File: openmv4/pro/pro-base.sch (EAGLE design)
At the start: 154 parts, among them J2 SAMTEC_FTSH-105-01-F-DVSAMTEC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, J6 2337019-1, M1 9774030243R, M2 9774030243R, Q1 BSS138, Q2 AO3401, U1 W25Q256JVEIQ_TR, U10 STM32H743IIK6, U11 TEXAS_INSTRUMENTS_BQ24072TRGT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, U14 IS42S32800, U2 EMIF06-MSD02N16, U3 ME6211C18M5G, U4 PAM2305AABADJ, U5 LSM6DS3TR-C, U6 MICROCHIP_USB3320C-EZK-TRMICR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, U7 LBEE5KL1DX-TEMP, U8 STMICROELECTRONICS_VL53L1CXV0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, U9 NXP_SEMICONDUCTORS_SE050C2HQ1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, X2 USD-1040310811, X3 DF12-36-DS, X4 S2B-PH-K-S(LF)(SN), Y0 SITIME_SIT1533AI-H4-DCC-32.76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, Y1 DSC1001BI1-024.0000

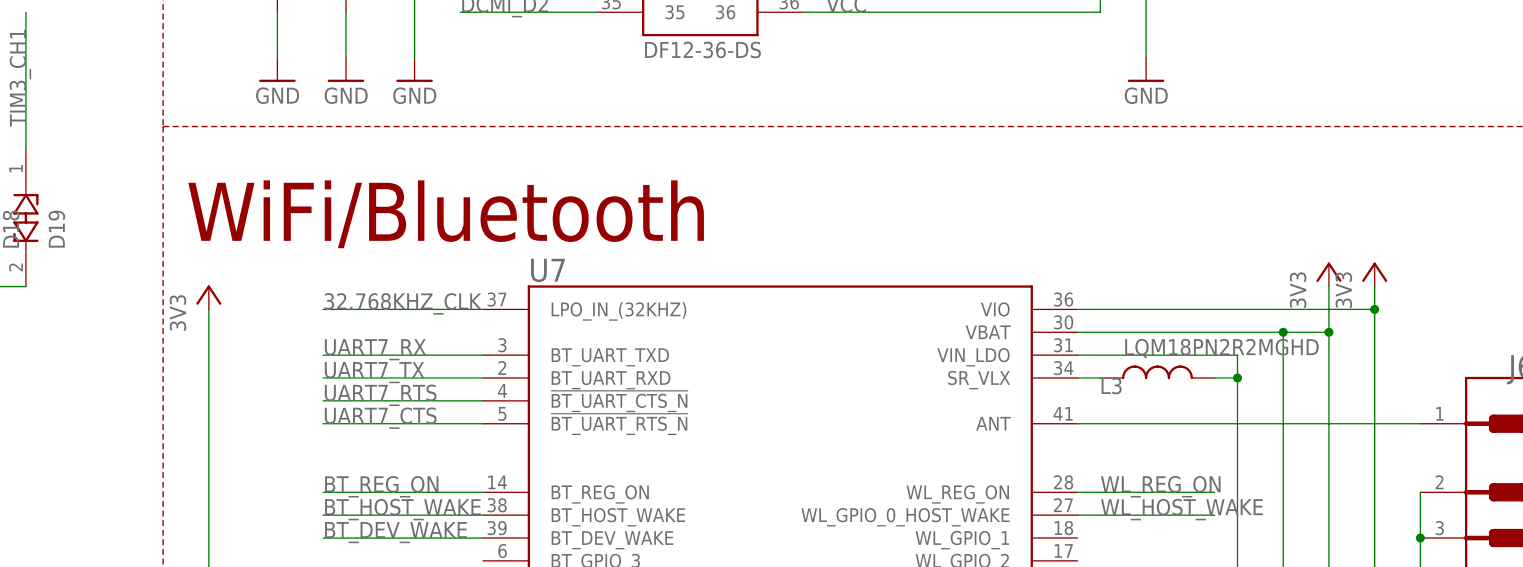
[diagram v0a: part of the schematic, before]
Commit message: Fix wifi power and tof location
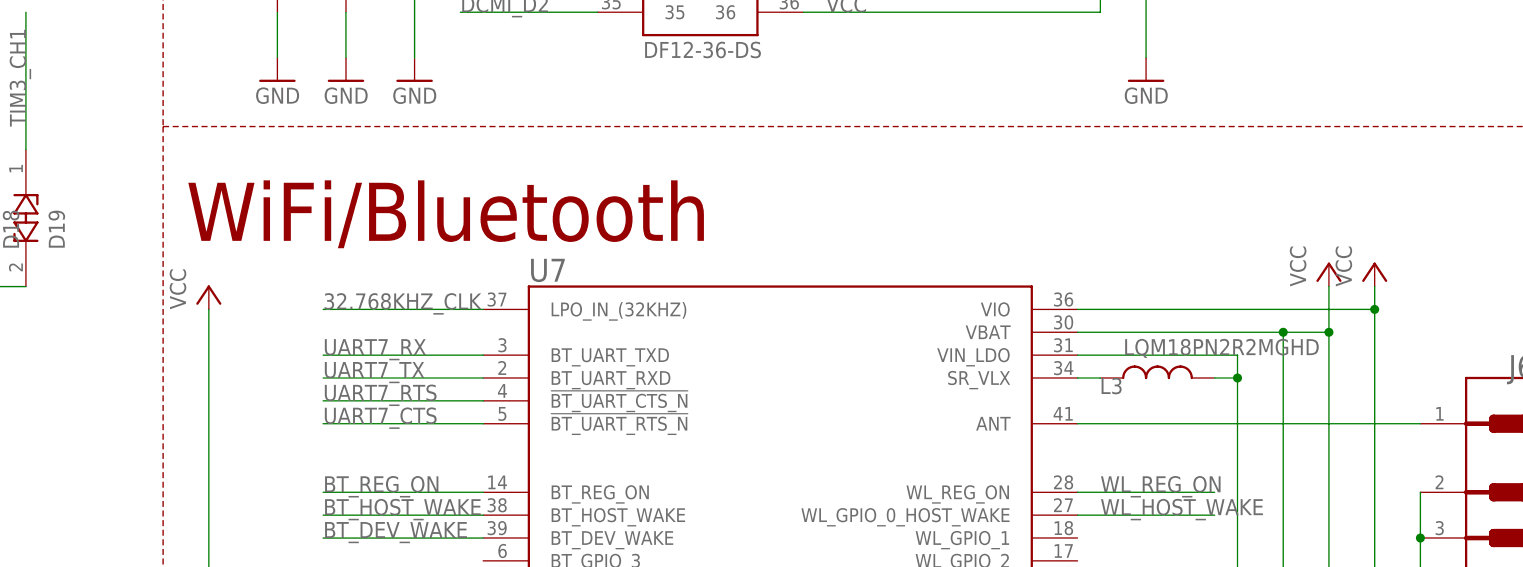
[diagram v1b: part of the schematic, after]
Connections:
- removed net 3V3: C38.1, C41.1, C42.1, C54.1, R14.2, R15.2, R16.2, R17.2, R9.2, U7.VBAT, U7.VIO
- net VCC: now also C38.1, C41.1, C42.1, C54.1, R14.2, R15.2, R16.2, R17.2, R9.2, U7.VBAT, U7.VIO
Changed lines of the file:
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@@
 <part name="R13" library="sfe" deviceset="RESISTOR" device="0402-RES" value="10K"/>
 <part name="U7" library="LBEE5KL1DX-TEMP" deviceset="LBEE5KL1DX-TEMP" device=""/>
-<part name="3V313" library="supply" deviceset="3V3" device=""/>
 <part name="C38" library="sfe" deviceset="CAP" device="0402-CAP" value="2.2uF"/>
 <part name="L3" library="sfe" deviceset="INDUCTOR" device="0603" value="LQM18PN2R2MGHD"/>
 <part name="GND32" library="sfe" deviceset="GND" device=""/>
-<part name="3V37" library="supply" deviceset="3V3" device=""/>
 <part name="R9" library="sfe" deviceset="RESISTOR" device="0402-RES" value="100K"/>
 <part name="R14" library="sfe" deviceset="RESISTOR" device="0402-RES" value="100K"/>
@@
 <part name="R16" library="sfe" deviceset="RESISTOR" device="0402-RES" value="100K"/>
 <part name="R17" library="sfe" deviceset="RESISTOR" device="0402-RES" value="100K"/>
-<part name="3V312" library="supply" deviceset="3V3" device=""/>
 <part name="C42" library="sfe" deviceset="CAP" device="0402-CAP" value="0.1uF"/>
 <part name="Y0" library="SiTime - SIT1533AI-H4-DCC-32.768E" deviceset="SITIME_SIT1533AI-H4-DCC-32.768E" device="SITIME_SIT1533AI-H4-DCC-32.768E_0_0"/>
@@
 <part name="R36" library="sfe" deviceset="RESISTOR" device="0402-RES" value="220"/>
 <part name="R37" library="sfe" deviceset="RESISTOR" device="0402-RES" value="220"/>
+<part name="P+31" library="supply1" library_urn="urn:adsk.eagle:library:371" deviceset="VCC" device=""/>
+<part name="P+32" library="supply1" library_urn="urn:adsk.eagle:library:371" deviceset="VCC" device=""/>
+<part name="P+33" library="supply1" library_urn="urn:adsk.eagle:library:371" deviceset="VCC" device=""/>
 </parts>
 <sheets>
@@
 <attribute name="VALUE" x="347.97" y="151.88" size="2.540909375" layer="96"/>
 </instance>
-<instance part="3V313" gate="G$1" x="441.96" y="215.9">
-<attribute name="VALUE" x="439.42" y="210.82" size="1.778" layer="96" rot="R90"/>
-</instance>
 <instance part="C38" gate="G$1" x="447.04" y="165.1" rot="MR0">
 <attribute name="NAME" x="445.516" y="168.021" size="1.778" layer="95" rot="MR90"/>
@@
 <attribute name="VALUE" x="454.66" y="149.86" size="1.778" layer="96" rot="MR0"/>
 </instance>
-<instance part="3V37" gate="G$1" x="312.42" y="213.36">
-<attribute name="VALUE" x="309.88" y="208.28" size="1.778" layer="96" rot="R90"/>
-</instance>
 <instance part="R9" gate="G$1" x="320.04" y="167.64" rot="R180">
 <attribute name="NAME" x="323.85" y="168.6814" size="1.778" layer="95" rot="R180"/>
@@
 <attribute name="VALUE" x="318.77" y="158.242" size="1.778" layer="96" rot="R180"/>
 </instance>
-<instance part="3V312" gate="G$1" x="436.88" y="215.9">
-<attribute name="VALUE" x="434.34" y="210.82" size="1.778" layer="96" rot="R90"/>
-</instance>
 <instance part="C42" gate="G$1" x="431.8" y="165.1" rot="MR0">
 <attribute name="NAME" x="430.276" y="168.021" size="1.778" layer="95" rot="MR90"/>
@@
 <attribute name="VALUE" x="323.85" y="409.702" size="1.778" layer="96" rot="R180"/>
 </instance>
+<instance part="P+31" gate="VCC" x="441.96" y="215.9">
+<attribute name="VALUE" x="439.42" y="213.36" size="1.778" layer="96" rot="R90"/>
+</instance>
+<instance part="P+32" gate="VCC" x="436.88" y="215.9">
+<attribute name="VALUE" x="434.34" y="213.36" size="1.778" layer="96" rot="R90"/>
+</instance>
+<instance part="P+33" gate="VCC" x="312.42" y="213.36">
+<attribute name="VALUE" x="309.88" y="210.82" size="1.778" layer="96" rot="R90"/>
+</instance>
 </instances>
 <busses>
@@
 <pinref part="D23" gate="G$0" pin="ANODE"/>
 </segment>
+<segment>
+<pinref part="U7" gate="G$1" pin="VIO"/>
+<wire x1="408.94" y1="210.82" x2="441.96" y2="210.82" width="0.1524" layer="91"/>
+<wire x1="441.96" y1="210.82" x2="441.96" y2="213.36" width="0.1524" layer="91"/>
+<junction x="441.96" y="210.82"/>
+<pinref part="C41" gate="G$1" pin="1"/>
+<wire x1="441.96" y1="170.18" x2="441.96" y2="172.72" width="0.1524" layer="91"/>
+<pinref part="C38" gate="G$1" pin="1"/>
+<wire x1="441.96" y1="172.72" x2="441.96" y2="210.82" width="0.1524" layer="91"/>
+<wire x1="447.04" y1="170.18" x2="447.04" y2="172.72" width="0.1524" layer="91"/>
+<wire x1="447.04" y1="172.72" x2="441.96" y2="172.72" width="0.1524" layer="91"/>
+<junction x="441.96" y="172.72"/>
+<pinref part="P+31" gate="VCC" pin="VCC"/>
+</segment>
+<segment>
+<pinref part="U7" gate="G$1" pin="VBAT"/>
+<wire x1="436.88" y1="208.28" x2="436.88" y2="170.18" width="0.1524" layer="91"/>
+<wire x1="408.94" y1="208.28" x2="431.8" y2="208.28" width="0.1524" layer="91"/>
+<wire x1="431.8" y1="208.28" x2="436.88" y2="208.28" width="0.1524" layer="91"/>
+<wire x1="436.88" y1="208.28" x2="436.88" y2="213.36" width="0.1524" layer="91"/>
+<junction x="436.88" y="208.28"/>
+<pinref part="C42" gate="G$1" pin="1"/>
+<wire x1="431.8" y1="170.18" x2="431.8" y2="208.28" width="0.1524" layer="91"/>
+<junction x="431.8" y="208.28"/>
+<pinref part="C54" gate="G$1" pin="1"/>
+<pinref part="P+32" gate="VCC" pin="VCC"/>
+</segment>
+<segment>
+<wire x1="314.96" y1="157.48" x2="312.42" y2="157.48" width="0.1524" layer="91"/>
+<wire x1="312.42" y1="157.48" x2="312.42" y2="160.02" width="0.1524" layer="91"/>
+<wire x1="312.42" y1="160.02" x2="312.42" y2="162.56" width="0.1524" layer="91"/>
+<wire x1="312.42" y1="162.56" x2="312.42" y2="165.1" width="0.1524" layer="91"/>
+<wire x1="312.42" y1="165.1" x2="312.42" y2="167.64" width="0.1524" layer="91"/>
+<wire x1="312.42" y1="167.64" x2="312.42" y2="210.82" width="0.1524" layer="91"/>
+<wire x1="314.96" y1="167.64" x2="312.42" y2="167.64" width="0.1524" layer="91"/>
+<wire x1="314.96" y1="165.1" x2="312.42" y2="165.1" width="0.1524" layer="91"/>
+<wire x1="314.96" y1="162.56" x2="312.42" y2="162.56" width="0.1524" layer="91"/>
+<wire x1="314.96" y1="160.02" x2="312.42" y2="160.02" width="0.1524" layer="91"/>
+<junction x="312.42" y="167.64"/>
+<junction x="312.42" y="165.1"/>
+<junction x="312.42" y="162.56"/>
+<junction x="312.42" y="160.02"/>
+<pinref part="R9" gate="G$1" pin="2"/>
+<pinref part="R14" gate="G$1" pin="2"/>
+<pinref part="R15" gate="G$1" pin="2"/>
+<pinref part="R16" gate="G$1" pin="2"/>
+<pinref part="R17" gate="G$1" pin="2"/>
+<pinref part="P+33" gate="VCC" pin="VCC"/>
+</segment>
 </net>
 <net name="DCMI_D0" class="5">
@@
 </segment>
 </net>
-<net name="3V3" class="0">
-<segment>
-<pinref part="3V312" gate="G$1" pin="3V3"/>
-<pinref part="U7" gate="G$1" pin="VBAT"/>
-<wire x1="436.88" y1="208.28" x2="436.88" y2="170.18" width="0.1524" layer="91"/>
-<wire x1="408.94" y1="208.28" x2="431.8" y2="208.28" width="0.1524" layer="91"/>
-<wire x1="431.8" y1="208.28" x2="436.88" y2="208.28" width="0.1524" layer="91"/>
-<wire x1="436.88" y1="208.28" x2="436.88" y2="213.36" width="0.1524" layer="91"/>
-<junction x="436.88" y="208.28"/>
-<pinref part="C42" gate="G$1" pin="1"/>
-<wire x1="431.8" y1="170.18" x2="431.8" y2="208.28" width="0.1524" layer="91"/>
-<junction x="431.8" y="208.28"/>
-<pinref part="C54" gate="G$1" pin="1"/>
-</segment>
-<segment>
-<pinref part="U7" gate="G$1" pin="VIO"/>
-<wire x1="408.94" y1="210.82" x2="441.96" y2="210.82" width="0.1524" layer="91"/>
-<wire x1="441.96" y1="210.82" x2="441.96" y2="213.36" width="0.1524" layer="91"/>
-<junction x="441.96" y="210.82"/>
-<pinref part="3V313" gate="G$1" pin="3V3"/>
-<pinref part="C41" gate="G$1" pin="1"/>
-<wire x1="441.96" y1="170.18" x2="441.96" y2="172.72" width="0.1524" layer="91"/>
-<pinref part="C38" gate="G$1" pin="1"/>
-<wire x1="441.96" y1="172.72" x2="441.96" y2="210.82" width="0.1524" layer="91"/>
-<wire x1="447.04" y1="170.18" x2="447.04" y2="172.72" width="0.1524" layer="91"/>
-<wire x1="447.04" y1="172.72" x2="441.96" y2="172.72" width="0.1524" layer="91"/>
-<junction x="441.96" y="172.72"/>
-</segment>
-<segment>
-<wire x1="314.96" y1="157.48" x2="312.42" y2="157.48" width="0.1524" layer="91"/>
-<wire x1="312.42" y1="157.48" x2="312.42" y2="160.02" width="0.1524" layer="91"/>
-<pinref part="3V37" gate="G$1" pin="3V3"/>
-<wire x1="312.42" y1="160.02" x2="312.42" y2="162.56" width="0.1524" layer="91"/>
-<wire x1="312.42" y1="162.56" x2="312.42" y2="165.1" width="0.1524" layer="91"/>
-<wire x1="312.42" y1="165.1" x2="312.42" y2="167.64" width="0.1524" layer="91"/>
-<wire x1="312.42" y1="167.64" x2="312.42" y2="210.82" width="0.1524" layer="91"/>
-<wire x1="314.96" y1="167.64" x2="312.42" y2="167.64" width="0.1524" layer="91"/>
-<wire x1="314.96" y1="165.1" x2="312.42" y2="165.1" width="0.1524" layer="91"/>
-<wire x1="314.96" y1="162.56" x2="312.42" y2="162.56" width="0.1524" layer="91"/>
-<wire x1="314.96" y1="160.02" x2="312.42" y2="160.02" width="0.1524" layer="91"/>
-<junction x="312.42" y="167.64"/>
-<junction x="312.42" y="165.1"/>
-<junction x="312.42" y="162.56"/>
-<junction x="312.42" y="160.02"/>
-<pinref part="R9" gate="G$1" pin="2"/>
-<pinref part="R14" gate="G$1" pin="2"/>
-<pinref part="R15" gate="G$1" pin="2"/>
-<pinref part="R16" gate="G$1" pin="2"/>
-<pinref part="R17" gate="G$1" pin="2"/>
-</segment>
-</net>

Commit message: Update pro
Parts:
- removed J6: 2337019-1, HIROSE - U.FL-R-SMT-1(10):HIROSE_U_FL-R-SMT-1_10HIROSE_U_FL-R-SMT-1_10_0_0
- added ANT1: 2450AT18B100E, 2450AT18B100E:2450AT18B100E
- added C39, C40, C55, C58, C59, C60, C61, C62, C63: 0.1uF, rcl:C-EUC0201
- added C64, C65: 4.7uF, SparkFun-Capacitors:4.7UF0603
- added C66, C67: 1.2pf, sfe:CAP0402-CAP
- added J7: MURATA_MM8130-2600RA2MURATA_MM8130-2600RA2_0_0, Murata - MM8130-2600RA2:MURATA_MM8130-2600RA2MURATA_MM8130-2600RA2_0_0
- added L4: 3.3nH, SparkFun-Coils:INDUCTOR-0402-3.9NH
- added R38: 220, sfe:RESISTOR0402-RES
- C26, C27, C28, C29, C30: device sfe:CAP0402-CAP -> rcl:C-EUC0201
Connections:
- removed net ANT: J6.SIG, U7.ANT
- new net ANT_PI_I: C66.1, L4.1, U7.ANT
- new net ANT_PI_O: C67.1, J7.IN, L4.2
- new net LED_IR_INT: Q1.G, R38.2
- new net N$1: ANT1.1, J7.OUT
- net GND: now also C39.2, C40.2, C55.2, C58.2, C59.2, C60.2, C61.2, C62.2, C63.2, C64.1, C65.1, C66.2, C67.2, J7.1_GROUND, J7.2_GROUND, J7.3_GROUND, J7.4_GROUND; no longer J6.1_GND, J6.2_GND
- net LED_IR: now also R38.1; no longer Q1.G
- net VCC: now also C39.1, C40.1, C55.1, C58.1, C59.1, C60.1, C61.1, C62.1, C63.1, C64.2, C65.2
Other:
- moved on the sheet: C26, C27, C28, C29, C30, C32, C33, C34, C35, C38, C41, C42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

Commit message: Update design
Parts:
- added C68: 0.1uF, sfe:CAP0402-CAP
- added U12: MICROCHIP_ATECC608A-SSHDA-BMICROCHIP_ATECC608A-SSHDA-B_0_0, Microchip - ATECC608A-SSHDA-B:MICROCHIP_ATECC608A-SSHDA-BMICROCHIP_ATECC608A-SSHDA-B_0_0
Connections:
- net GND: now also C68.2, U12.GND
- net I2C4_SCL: now also U12.SCL
- net I2C4_SDA: now also U12.SDA
- net VCC: now also C68.1
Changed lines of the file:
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@@
 <part name="L4" library="SparkFun-Coils" library_urn="urn:adsk.eagle:library:512" deviceset="INDUCTOR" device="-0402-3.9NH" package3d_urn="urn:adsk.eagle:package:37575/1" value="3.3nH"/>
 <part name="ANT1" library="2450AT18B100E" deviceset="2450AT18B100E" device=""/>
+<part name="U12" library="Microchip - ATECC608A-SSHDA-B" deviceset="MICROCHIP_ATECC608A-SSHDA-B" device="MICROCHIP_ATECC608A-SSHDA-B_0_0"/>
+<part name="P+34" library="supply1" library_urn="urn:adsk.eagle:library:371" deviceset="VCC" device=""/>
+<part name="GND54" library="sfe" deviceset="GND" device=""/>
+<part name="C68" library="sfe" deviceset="CAP" device="0402-CAP" value="0.1uF"/>
+<part name="GND57" library="sfe" deviceset="GND" device=""/>
 </parts>
 <sheets>
@@
 <attribute name="VALUE" x="454.66" y="91.44" size="1.778" layer="95" rot="R90"/>
 </instance>
+<instance part="U12" gate="G$0" x="264.16" y="172.72" smashed="yes">
+<attribute name="NAME" x="266.7" y="170.18" size="2.54" layer="95" align="top-left"/>
+</instance>
+<instance part="P+34" gate="VCC" x="259.08" y="170.18" smashed="yes">
+<attribute name="VALUE" x="256.54" y="167.64" size="1.778" layer="96" rot="R90"/>
+</instance>
+<instance part="GND54" gate="1" x="289.56" y="142.24" smashed="yes" rot="MR0">
+<attribute name="VALUE" x="292.1" y="139.7" size="1.778" layer="96" rot="MR0"/>
+</instance>
+<instance part="C68" gate="G$1" x="259.08" y="157.48" smashed="yes" rot="MR0">
+<attribute name="NAME" x="257.556" y="160.401" size="1.778" layer="95" rot="MR0"/>
+<attribute name="VALUE" x="257.556" y="155.321" size="1.778" layer="96" rot="MR0"/>
+</instance>
+<instance part="GND57" gate="1" x="259.08" y="142.24" smashed="yes" rot="MR0">
+<attribute name="VALUE" x="261.62" y="139.7" size="1.778" layer="96" rot="MR0"/>
+</instance>
 </instances>
 <busses>
@@
 <wire x1="469.9" y1="45.72" x2="469.9" y2="48.26" width="0.1524" layer="91"/>
 </segment>
+<segment>
+<pinref part="GND54" gate="1" pin="GND"/>
+<pinref part="U12" gate="G$0" pin="GND"/>
+<wire x1="289.56" y1="144.78" x2="289.56" y2="147.32" width="0.1524" layer="91"/>
+</segment>
+<segment>
+<pinref part="GND57" gate="1" pin="GND"/>
+<pinref part="C68" gate="G$1" pin="2"/>
+<wire x1="259.08" y1="144.78" x2="259.08" y2="154.94" width="0.1524" layer="91"/>
+</segment>
 </net>
 <net name="NRST" class="0">
@@
 <junction x="480.06" y="60.96"/>
 </segment>
+<segment>
+<pinref part="C68" gate="G$1" pin="1"/>
+<pinref part="P+34" gate="VCC" pin="VCC"/>
+<wire x1="259.08" y1="162.56" x2="259.08" y2="167.64" width="0.1524" layer="91"/>
+</segment>
 </net>
 <net name="DCMI_D0" class="5">
@@
 <label x="116.84" y="330.2" size="1.778" layer="95"/>
 </segment>
+<segment>
+<wire x1="289.56" y1="165.1" x2="299.72" y2="165.1" width="0.1524" layer="91"/>
+<pinref part="U12" gate="G$0" pin="SCL"/>
+<label x="292.1" y="165.1" size="1.778" layer="95"/>
+</segment>
 </net>
 <net name="I2C4_SDA" class="0">
@@
 <label x="116.84" y="327.66" size="1.778" layer="95"/>
 </segment>
+<segment>
+<wire x1="289.56" y1="162.56" x2="299.72" y2="162.56" width="0.1524" layer="91"/>
+<pinref part="U12" gate="G$0" pin="SDA"/>
+<label x="292.1" y="162.56" size="1.778" layer="95"/>
+</segment>
 </net>

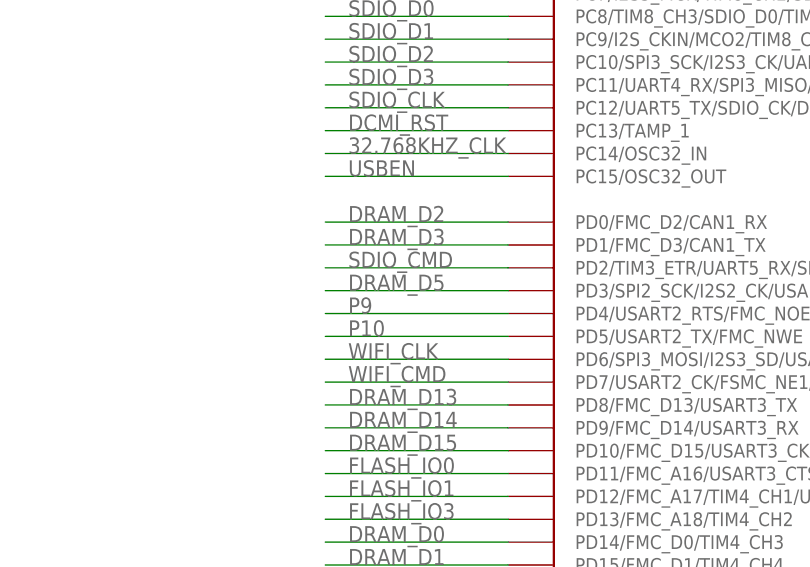
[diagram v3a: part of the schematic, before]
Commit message: Fix pin naming
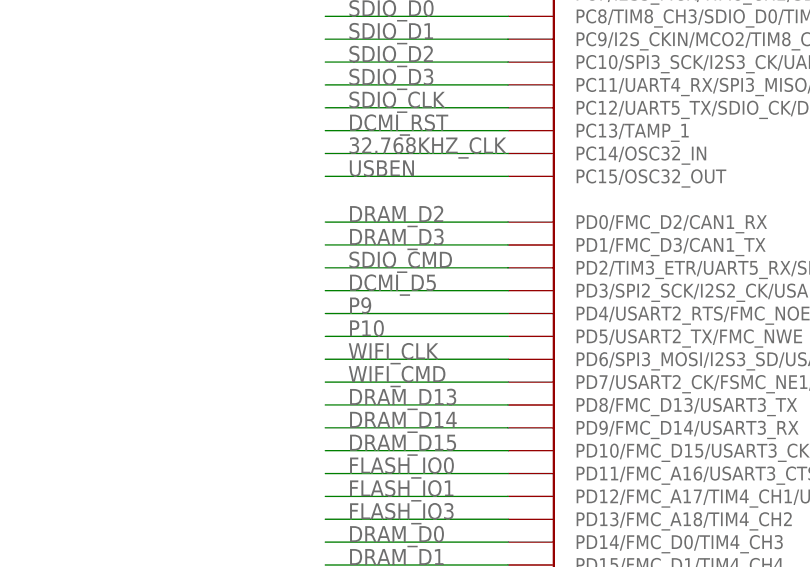
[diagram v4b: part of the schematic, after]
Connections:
- net DCMI_D5: now also U10.PD3/SPI2_SCK/I2S2_CK/USART2_CTS/FMC_CLK/DCMI_D5
- net DRAM_D5: no longer U10.PD3/SPI2_SCK/I2S2_CK/USART2_CTS/FMC_CLK/DCMI_D5
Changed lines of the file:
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@@
 <pinref part="X3" gate="G$1" pin="33"/>
+</segment>
+<segment>
+<pinref part="U10" gate="G$2" pin="PD3/SPI2_SCK/I2S2_CK/USART2_CTS/FMC_CLK/DCMI_D5"/>
+<wire x1="66.04" y1="78.74" x2="45.72" y2="78.74" width="0.1524" layer="91"/>
+<label x="48.26" y="78.74" size="1.778" layer="95"/>
 </segment>
 </net>
@@
 <pinref part="U10" gate="G$2" pin="PE8/FSMC_D5/TIM1_CH1N/UART7_TX"/>
 </segment>
-<segment>
-<pinref part="U10" gate="G$2" pin="PD3/SPI2_SCK/I2S2_CK/USART2_CTS/FMC_CLK/DCMI_D5"/>
-<wire x1="66.04" y1="78.74" x2="45.72" y2="78.74" width="0.1524" layer="91"/>
-<label x="48.26" y="78.74" size="1.778" layer="95"/>
-</segment>
-</net>
+</net>

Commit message: Remove NXP chip
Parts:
- removed C49, C50: 0.1uF, sfe:CAP0402-CAP
- removed R28: 100K, sfe:RESISTOR0402-RES
- removed U9: NXP_SEMICONDUCTORS_SE050C2HQ1-Z01SDZNXP_SEMICONDUCTORS_SE05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, Z01SDZ:NXP_SEMICONDUCTORS_SE050C2HQ1-Z01SDZNXP_SEMICONDUCTORS_SE050C2HQ1-Z01SDZ_0_1
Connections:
- net CRYPTOEN: no longer R28.2, U9.ENA
- net GND: no longer C49.2, C50.2, R28.1, U9.EP, U9.ISO_14443_LA, U9.ISO_14443_LB, U9.VSS
- net I2C4_SCL: no longer U9.I2C_SCL
- net I2C4_SDA: no longer U9.I2C_SDA
- net VCC: no longer C49.1, C50.1, U9.ISO_7816_!RST!, U9.ISO_7816_CLK, U9.ISO_7816_IO1, U9.ISO_7816_IO2, U9.VCC, U9.VIN, U9.VOUT
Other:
- moved on the sheet: C68, U12
